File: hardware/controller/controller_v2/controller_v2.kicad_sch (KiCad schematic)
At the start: 22 parts, among them J1 USB_C_Receptacle_USB2.0_16P, J2 Conn_01x04_Socket, SW1 SW_Push, SW2 SW_Push, U1 ESP32-C3-MINI-1-N4, U2 74AHCT1G125, U4 AMS1117-3.3

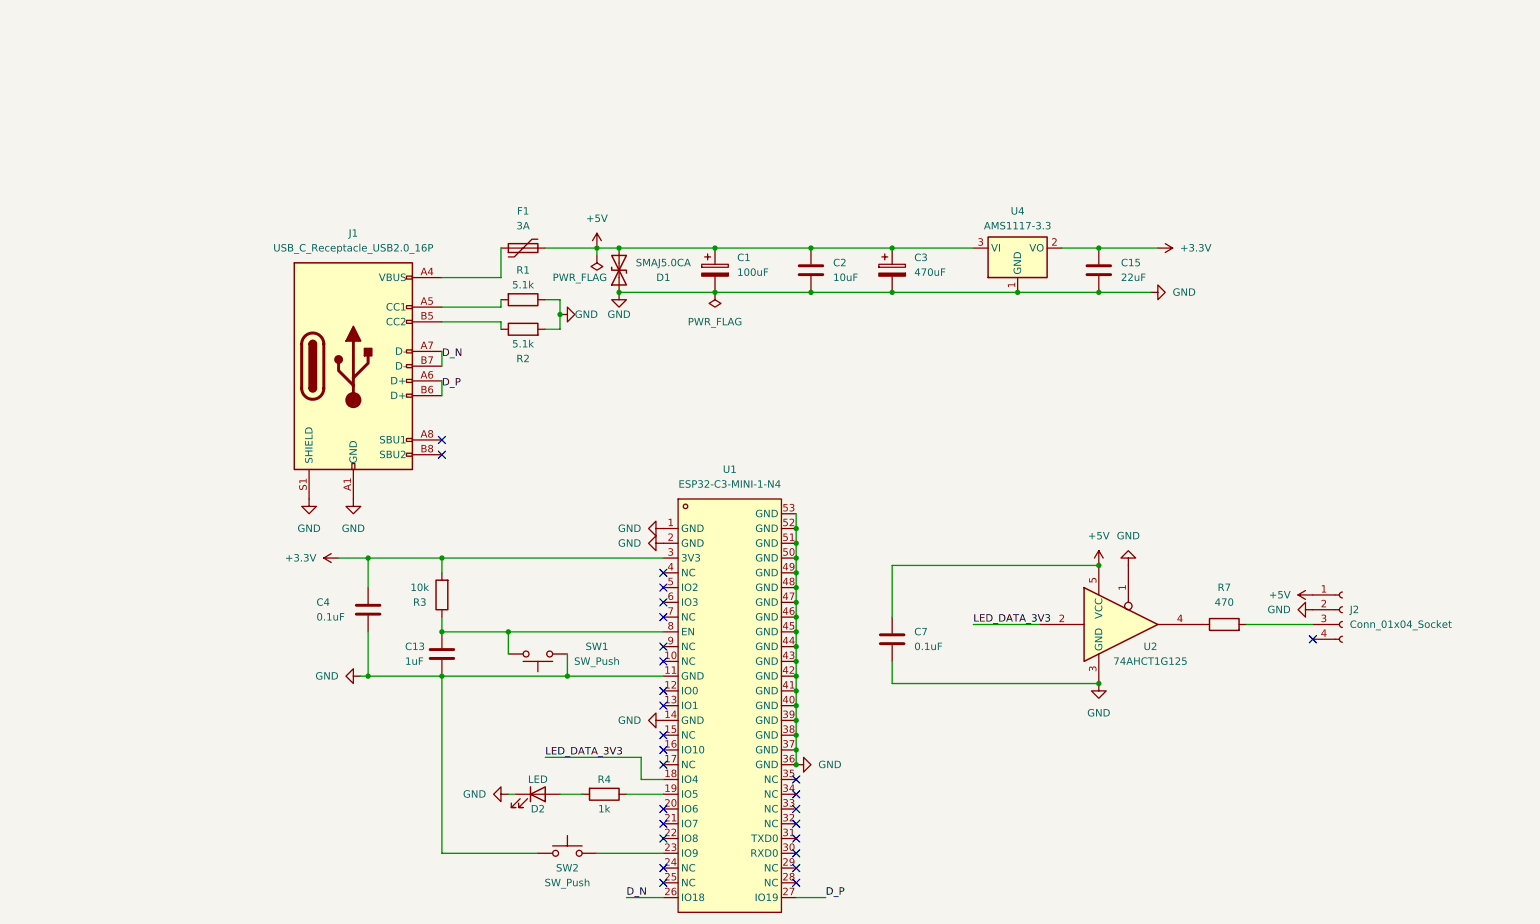
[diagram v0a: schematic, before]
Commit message: Hardware: finalize controller v2 + add octave-flex design
Controller v2 (ready for JLCPCB assembly):
- DRC clean, all clearance/footprint issues resolved
- U3 (TS3USB221A QFN-10) fine-pitch handling: local clearance override + solder_mask_margin=0 on all pads
- J4 PJ-320A footprint update + mechanical pad fix (1.2mm -> 1.6mm)
- C14 removed (redundant with C3 470uF bulk near J2)
- BOM verified with LCSC part numbers, all 26 SMT parts vetted for JLC matching
- Gerbers + production files exported via Fabrication Toolkit

New octave-flex design (replaces 5x rigid octave-module):
- Single 829.35 x 10.69 mm flex PCB, 60 LEDs at 13.75mm uniform spacing
- WS2812B 5050 footprint, J1 (JST SH 4P) connector at left edge
- GND zone (hatched, 45-degree, 0.5/0.5mm) on B.Cu - flex-compatible
- FR-4 stiffener spec under J1 for PCBWay
- 60 LED + 60 cap + 1 connector hand-solderable

BOM.csv updates:
- C3 promoted to 470uF aluminum bulk (was 0.1uF spare)
- C7 added as spare 5V decoupling
- Octave entries replaced: D1-D60 + C1-C60 + J1 single flex board
- Cabling: 5 cables -> 1 cable (single strip vs 5 boards)

Co-Authored-By: Claude Opus 4.7 <noreply@anthropic.com>
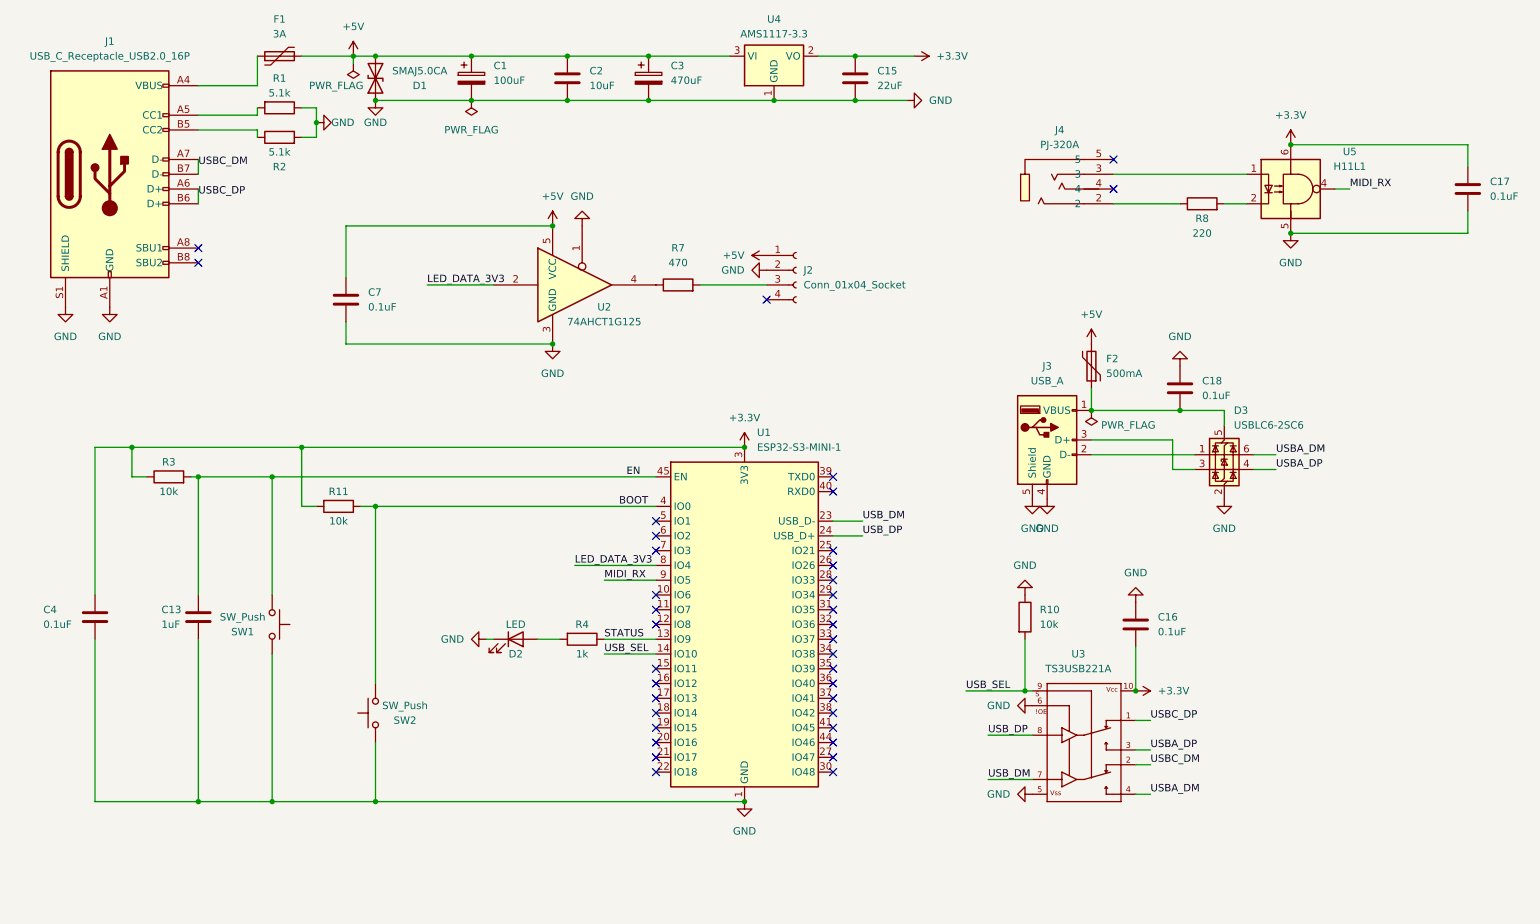
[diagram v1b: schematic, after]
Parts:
- removed U1: ESP32-C3-MINI-1-N4, ESP32-C3-MINI-1:WIFIM-SMD_ESP32-C3-MINI-1, symbol ESP32-C3-MINI-1:ESP32-C3-MINI-1-N4
- added C16, C17, C18: 0.1uF, Capacitor_SMD:C_0603_1608Metric, symbol Device:C
- added D3: USBLC6-2SC6, Package_TO_SOT_SMD:SOT-23-6, symbol Power_Protection:USBLC6-2SC6
- added F2: 500mA, Fuse:Fuse_1206_3216Metric, symbol Device:Polyfuse
- added J3: USB_A, Connector_USB:USB_A_TE_292303-7_Horizontal, symbol Connector:USB_A
- added J4: PJ-320A, easyeda2kicad:AUDIO-TH_XKB_PJ-320A, symbol easyeda2kicad:PJ-320A
- added R10, R11: 10k, Resistor_SMD:R_0603_1608Metric, symbol Device:R
- added R8: 220, Resistor_SMD:R_0603_1608Metric, symbol Device:R
- added U1: ESP32-S3-MINI-1, RF_Module:ESP32-S2-MINI-1, symbol RF_Module:ESP32-S3-MINI-1
- added U3: TS3USB221A, TS3USB221A:QFN-10-RSE, symbol TS3USB221A:TS3USB221A
- added U5: H11L1, H11L1SM:IC_H11L1SM, symbol Isolator:H11L1
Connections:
- net +3.3V: now also R3.1, C16.2, C17.2, R11.2, U1.3 (3V3), U3.10, U5.6; no longer R3.2
- net +5V: now also F2.2
- net GND: now also SW1.2, C16.1, C17.1, C18.2, D3.2 (GND), J3.4 (GND), J3.5 (Shield), R10.1, U1.1 (GND), U1.2 (GND), U1.42 (GND), U1.43 (GND), U1.46 (GND), U1.47 (GND), U1.48 (GND), U1.49 (GND), U1.50 (GND), U1.51 (GND), U1.52 (GND), U1.53 (GND), U1.54 (GND), U1.55 (GND), U1.56 (GND), U1.57 (GND), U1.58 (GND), U1.59 (GND), U1.60 (GND), U1.61 (GND), U1.62 (GND), U1.63 (GND), U1.64 (GND), U1.65 (GND), U3.5, U3.6, U5.5; no longer SW1.1
- net LED_DATA_3V3: now also U1.8 (IO4)
- net STATUS: now reaches R4.1
- net STATUS: now also U1.13 (IO9)
- net BOOT: now reaches SW2.2
- net BOOT: now also R11.1, U1.4 (IO0)
- net D_N renamed USBC_DM
- net USBC_DM: now also U3.2
- net D_P renamed USBC_DP
- net USBC_DP: now also U3.1
- new net: C18.1, D3.5 (VBUS), F2.1, J3.1 (VBUS)
- new net: D3.1 (I/O1), J3.2 (D-)
- new net: D3.3 (I/O2), J3.3 (D+)
- new net: J4.2, R8.1
- new net: J4.3, U5.1
- new net: R8.2, U5.2
- new net EN: C13.1, R3.2, SW1.1, U1.45 (EN)
- new net MIDI_RX: U1.9 (IO5), U5.4
- new net USBA_DM: D3.6 (I/O1), U3.4
- new net USBA_DP: D3.4 (I/O2), U3.3
- new net USB_DM: U1.23 (USB_D-), U3.7
- new net USB_DP: U1.24 (USB_D+), U3.8
- new net USB_SEL: R10.2, U1.14 (IO10), U3.9
- no-connect marks 27 -> 37
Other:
- moved on the sheet: C1, C13, C15, C2, C3, C4, C7, D1, D2, F1, J1, J2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

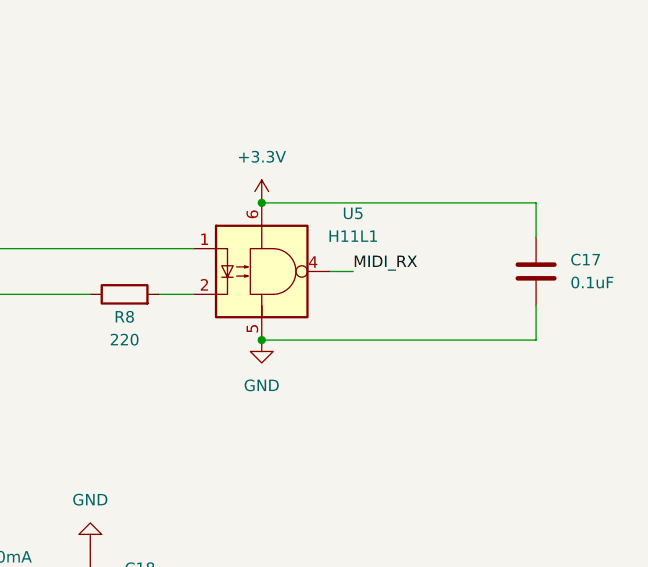
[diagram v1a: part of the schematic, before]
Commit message: Octave-module flex PCB ready for fab; checkpoint full repo
hardware/octave-module: uniform 13.708 mm LED pitch (caps aligned), solder lap-seam (J2 output / J3 input pads), J2 plated 0.8 mm solder-access holes, full routing + GND pour, J1 placement; seam-lap footprint library; spacing/seam design docs; regenerated BOM + production files (J1 DNP, caps C14663, LEDs C2761795).
Also includes controller_v2, mobile app, backend, and project-doc updates.

Co-Authored-By: Claude Opus 4.8 <noreply@anthropic.com>
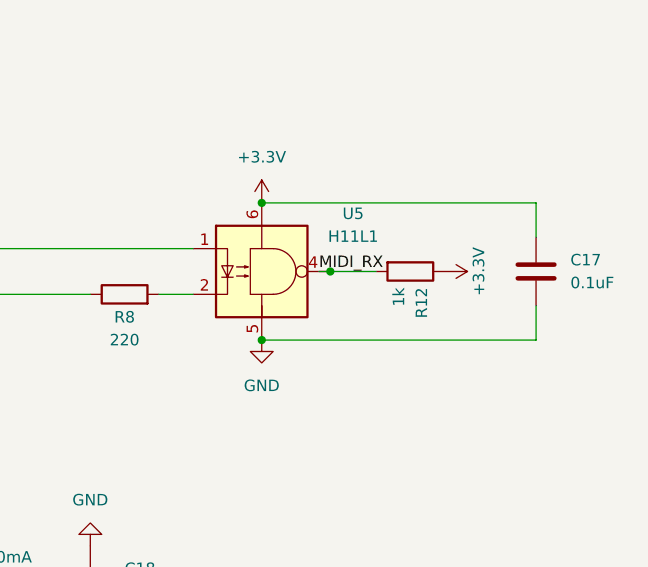
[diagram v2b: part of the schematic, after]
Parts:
- added R12: 1k, Resistor_SMD:R_0603_1608Metric, symbol Device:R
- J3: footprint Connector_USB:USB_A_TE_292303-7_Horizontal -> easyeda2kicad:USB-A-TH__USB-AF-90
- SW1, SW2: footprint Button_Switch_SMD:SW_SPST_PTS645Sx43SMTR92 -> easyeda2kicad:SW-SMD_4P-L5.1-W5.1-P3.70-LS6.5-TL_H1.5
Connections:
- net +3.3V: now also R12.1
- net MIDI_RX: now also R12.2
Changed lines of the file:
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@@
 	)
 	(junction
+		(at 292.1 66.04)
+		(diameter 0)
+		(color 0 0 0 0)
+	)
+	(junction
 		(at 109.22 115.57)
 		(diameter 0)
@@
 	(wire
 		(pts
-			(xy 294.64 66.04) (xy 292.1 66.04)
+			(xy 292.1 66.04) (xy 297.18 66.04)
 		)
 		(stroke
@@
 		)
 	)
+	(wire
+		(pts
+			(xy 290.83 66.04) (xy 292.1 66.04)
+		)
+		(stroke
+			(width 0)
+			(type default)
+		)
+	)
 	(label "USBA_DM"
 		(at 281.94 111.76 0)
@@
 	)
 	(label "MIDI_RX"
-		(at 294.64 66.04 0)
+		(at 290.83 66.04 0)
 		(effects
 			(font
@@
 			)
 		)
-		(property "Footprint" "Button_Switch_SMD:SW_SPST_PTS645Sx43SMTR92"
+		(property "Footprint" "easyeda2kicad:SW-SMD_4P-L5.1-W5.1-P3.70-LS6.5-TL_H1.5"
 			(at 114.3 140.97 0)
 			(effects
@@
 	)
 	(symbol
+		(lib_id "Device:R")
+		(at 300.99 66.04 270)
+		(unit 1)
+		(exclude_from_sim no)
+		(in_bom yes)
+		(on_board yes)
+		(dnp no)
+		(property "Reference" "R12"
+			(at 302.26 67.82 0)
+			(effects
+				(font
+					(size 1.27 1.27)
+				)
+				(justify left)
+			)
+		)
+		(property "Value" "1k"
+			(at 299.72 67.82 0)
+			(effects
+				(font
+					(size 1.27 1.27)
+				)
+				(justify left)
+			)
+		)
+		(property "Footprint" "Resistor_SMD:R_0603_1608Metric"
+			(at 300.99 64.262 90)
+			(effects
+				(font
+					(size 1.27 1.27)
+				)
+				(hide yes)
+			)
+		)
+		(property "Datasheet" "~"
+			(at 300.99 66.04 0)
+			(effects
+				(font
+					(size 1.27 1.27)
+				)
+				(hide yes)
+			)
+		)
+		(property "Description" ""
+			(at 300.99 66.04 0)
+			(effects
+				(font
+					(size 1.27 1.27)
+				)
+			)
+		)
+		(pin "2"
+		)
+		(pin "1"
+		)
+		(instances
+			(project ""
+				(path "/ac32532a-240d-4791-8a1e-f1f3661d70e1"
+					(reference "R12")
+					(unit 1)
+				)
+			)
+		)
+	)
+	(symbol
 		(lib_id "Connector:USB_A")
 		(at 242.57 109.22 0)
@@
 			)
 		)
-		(property "Footprint" "Connector_USB:USB_A_TE_292303-7_Horizontal"
+		(property "Footprint" "easyeda2kicad:USB-A-TH__USB-AF-90"
 			(at 246.38 110.49 0)
 			(effects
@@
 	)
 	(symbol
+		(lib_id "power:+3.3V")
+		(at 304.8 66.04 270)
+		(unit 1)
+		(exclude_from_sim no)
+		(in_bom yes)
+		(on_board yes)
+		(dnp no)
+		(property "Reference" "#PWR0100"
+			(at 300.99 66.04 0)
+			(effects
+				(font
+					(size 1.27 1.27)
+				)
+				(hide yes)
+			)
+		)
+		(property "Value" "+3.3V"
+			(at 308.61 66.04 0)
+			(effects
+				(font
+					(size 1.27 1.27)
+				)
+			)
+		)
+		(property "Footprint" ""
+			(at 304.8 66.04 0)
+			(effects
+				(font
+					(size 1.27 1.27)
+				)
+				(hide yes)
+			)
+		)
+		(property "Datasheet" ""
+			(at 304.8 66.04 0)
+			(effects
+				(font
+					(size 1.27 1.27)
+				)
+				(hide yes)
+			)
+		)
+		(property "Description" ""
+			(at 304.8 66.04 0)
+			(effects
+				(font
+					(size 1.27 1.27)
+				)
+			)
+		)
+		(pin "1"
+		)
+		(instances
+			(project ""
+				(path "/ac32532a-240d-4791-8a1e-f1f3661d70e1"
+					(reference "#PWR0100")
+					(unit 1)
+				)
+			)
+		)
+	)
+	(symbol
 		(lib_id "power:PWR_FLAG")
 		(at 250.19 104.14 180)
@@
 			)
 		)
-		(property "Footprint" "Button_Switch_SMD:SW_SPST_PTS645Sx43SMTR92"
+		(property "Footprint" "easyeda2kicad:SW-SMD_4P-L5.1-W5.1-P3.70-LS6.5-TL_H1.5"
 			(at 121.92 156.21 0)
 			(effects
